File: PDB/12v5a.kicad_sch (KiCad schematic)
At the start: 28 parts, among them M3 CSD19502Q5B, M4 CSD17578Q3A, U21 LM5118MH/NOPB

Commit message: Finished all the footprints. doing poe myself now
finally.
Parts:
- added C40: 100nf, Capacitor_SMD:C_0603_1608Metric, symbol Device:C
- added D23: LED, LED_SMD:LED_0805_2012Metric, symbol Device:LED
- added F6: TR/3216FF15-R, Fuse:Fuse_1206_3216Metric, symbol Device:Fuse
- added R45: R_Shunt, Resistor_SMD:R_0603_1608Metric, symbol Device:R_Shunt
- added R46: 270, Capacitor_SMD:C_0603_1608Metric, symbol Device:R
- added TP11: TestPoint, TestPoint:TestPoint_Pad_D2.0mm, symbol Connector:TestPoint
- added U22: INA228, Package_SO:HVSSOP-10-1EP_3x3mm_P0.5mm_EP1.83x1.89mm, symbol Sensor_Energy:INA228
- Cboot4: renamed from Cboot1; footprint (none) -> Capacitor_SMD:C_0603_1608Metric
- Ccomp5: renamed from Ccomp3; footprint (none) -> Capacitor_SMD:C_0603_1608Metric
- Ccomp6: renamed from Ccomp4; footprint (none) -> Capacitor_SMD:C_0603_1608Metric
- Cin5: renamed from Cin1; footprint (none) -> Capacitor_SMD:C_0603_1608Metric
- Cin_1: renamed from Cin_2; footprint (none) -> Capacitor_SMD:C_0603_1608Metric
- Cin_2: renamed from Cin_3; footprint (none) -> Capacitor_SMD:C_0603_1608Metric
- Cinx4: renamed from Cinx1; footprint (none) -> Capacitor_SMD:C_0603_1608Metric
- Cout5: renamed from Cout1; footprint (none) -> Capacitor_SMD:C_0603_1608Metric
- Cout_2: renamed from Cout_3; footprint (none) -> Capacitor_SMD:C_0603_1608Metric
- Coutx4: renamed from Coutx3; footprint (none) -> Capacitor_SMD:C_0603_1608Metric
- Coutx5: renamed from Coutx4; footprint (none) -> Capacitor_SMD:C_0603_1608Metric
- Cramp3: renamed from Cramp1; footprint (none) -> Capacitor_SMD:C_0603_1608Metric
- Css3: renamed from Css1; footprint (none) -> Capacitor_SMD:C_0603_1608Metric
- Cvcc4: renamed from Cvcc1; footprint (none) -> Capacitor_SMD:C_0603_1608Metric
- D21: renamed from D20; footprint (none) -> Package_TO_SOT_SMD:TO-252-2_TabPin1
- D22: renamed from D21; footprint (none) -> Diode_THT:D_5W_P10.16mm_Horizontal
- L7: renamed from L4; footprint (none) -> Inductor_SMD:L_1206_3216Metric
- M3, M4: footprint (none) -> Dependencies:CSD19502Q5B
- Rcomp3: renamed from Rcomp1; footprint (none) -> Resistor_SMD:R_0603_1608Metric
- Renable3: renamed from Renable1; footprint (none) -> Resistor_SMD:R_0603_1608Metric
- Rfbb5: renamed from Rfbb1; footprint (none) -> Resistor_SMD:R_0603_1608Metric
- Rfbt5: renamed from Rfbt1; footprint (none) -> Resistor_SMD:R_0603_1608Metric
- Rsense3: renamed from Rsense1; footprint (none) -> Resistor_SMD:R_0603_1608Metric
- Rt3: renamed from Rt1; footprint (none) -> Resistor_SMD:R_0603_1608Metric
- Ruv5: renamed from Ruv3; footprint (none) -> Resistor_SMD:R_0603_1608Metric
- Ruv6: renamed from Ruv4; footprint (none) -> Resistor_SMD:R_0603_1608Metric
- U21: footprint (none) -> Dependencies:LM5118MH
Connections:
- net 12V@5A: now also R45.4, R46.1, TP11.1; no longer Cout5.1 (+), Cout_2.1 (+), Coutx4.1, Coutx5.1, D22.1 (K), Rfbt5.1, U21.10 (VOUT)
- net GND: now also C40.1, D23.1 (K), U22.1 (A1), U22.2 (A0), U22.7 (GND)
- new net: Cout5.1 (+), Cout_2.1 (+), Coutx4.1, Coutx5.1, D22.1 (K), F6.1, Rfbt5.1, U21.10 (VOUT)
- new net: D23.2 (A), R46.2
- new net: F6.2, R45.1, U22.8 (Vbus)
- new net: R45.2, U22.10 (Vin+)
- new net: R45.3, U22.9 (Vin-)
- new net +3.3V: C40.2, U22.6 (VS)
- new net SCL: U22.5 (SCL)
- new net SDA: U22.4 (SDA)
- no-connect marks 0 -> 1

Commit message: fixed component footprints
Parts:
- R45: footprint Resistor_SMD:R_0603_1608Metric -> Resistor_SMD:R_Shunt_Vishay_WSR2_WSR3_KelvinConnection
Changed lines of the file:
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@@
 		(dnp no)
 		(fields_autoplaced yes)
-		(property "Reference" "#PWR086"
+		(property "Reference" "#PWR097"
 			(at 524.51 81.28 0)
 			(hide yes)
@@
 			(project "PDB"
 				(path "/a9cf05c4-aac5-4cf1-b700-1d3045f8dfbd/9aa37ff9-47e7-4c71-b8fb-21d9fa084287"
-					(reference "#PWR086")
+					(reference "#PWR097")
 					(unit 1)
 				)
@@
 		(dnp no)
 		(fields_autoplaced yes)
-		(property "Reference" "#PWR082"
+		(property "Reference" "#PWR095"
 			(at 332.74 220.98 0)
 			(hide yes)
@@
 			(project "PDB"
 				(path "/a9cf05c4-aac5-4cf1-b700-1d3045f8dfbd/9aa37ff9-47e7-4c71-b8fb-21d9fa084287"
-					(reference "#PWR082")
+					(reference "#PWR095")
 					(unit 1)
 				)
@@
 		(dnp no)
 		(fields_autoplaced yes)
-		(property "Reference" "#PWR089"
+		(property "Reference" "#PWR0100"
 			(at 571.5 130.81 0)
 			(hide yes)
@@
 			(project "PDB"
 				(path "/a9cf05c4-aac5-4cf1-b700-1d3045f8dfbd/9aa37ff9-47e7-4c71-b8fb-21d9fa084287"
-					(reference "#PWR089")
+					(reference "#PWR0100")
 					(unit 1)
 				)
@@
 		(dnp no)
 		(fields_autoplaced yes)
-		(property "Reference" "#PWR087"
+		(property "Reference" "#PWR098"
 			(at 554.99 99.06 0)
 			(hide yes)
@@
 			(project "PDB"
 				(path "/a9cf05c4-aac5-4cf1-b700-1d3045f8dfbd/9aa37ff9-47e7-4c71-b8fb-21d9fa084287"
-					(reference "#PWR087")
+					(reference "#PWR098")
 					(unit 1)
 				)
@@
 		(dnp no)
 		(fields_autoplaced yes)
-		(property "Reference" "#PWR083"
+		(property "Reference" "#PWR099"
 			(at 548.64 121.92 0)
 			(hide yes)
@@
 			(project "PDB"
 				(path "/a9cf05c4-aac5-4cf1-b700-1d3045f8dfbd/9aa37ff9-47e7-4c71-b8fb-21d9fa084287"
-					(reference "#PWR083")
+					(reference "#PWR099")
 					(unit 1)
 				)
@@
 			)
 		)
-		(property "Footprint" "Resistor_SMD:R_0603_1608Metric"
+		(property "Footprint" "Resistor_SMD:R_Shunt_Vishay_WSR2_WSR3_KelvinConnection"
 			(at 534.67 119.888 90)
 			(hide yes)
@@
 		(dnp no)
 		(fields_autoplaced yes)
-		(property "Reference" "#PWR085"
+		(property "Reference" "#PWR094"
 			(at 297.18 101.6 0)
 			(hide yes)
@@
 			(project "PDB"
 				(path "/a9cf05c4-aac5-4cf1-b700-1d3045f8dfbd/9aa37ff9-47e7-4c71-b8fb-21d9fa084287"
-					(reference "#PWR085")
+					(reference "#PWR094")
 					(unit 1)
 				)
@@
 		(dnp no)
 		(fields_autoplaced yes)
-		(property "Reference" "#PWR081"
+		(property "Reference" "#PWR096"
 			(at 514.35 115.57 0)
 			(hide yes)
@@
 			(project "PDB"
 				(path "/a9cf05c4-aac5-4cf1-b700-1d3045f8dfbd/9aa37ff9-47e7-4c71-b8fb-21d9fa084287"
-					(reference "#PWR081")
+					(reference "#PWR096")
 					(unit 1)
 				)
@@
 		(dnp no)
 		(fields_autoplaced yes)
-		(property "Reference" "#PWR084"
+		(property "Reference" "#PWR093"
 			(at 229.87 256.54 0)
 			(hide yes)
@@
 			(project "PDB"
 				(path "/a9cf05c4-aac5-4cf1-b700-1d3045f8dfbd/9aa37ff9-47e7-4c71-b8fb-21d9fa084287"
-					(reference "#PWR084")
+					(reference "#PWR093")
 					(unit 1)
 				)
@@
 		(dnp no)
 		(fields_autoplaced yes)
-		(property "Reference" "#PWR080"
+		(property "Reference" "#PWR092"
 			(at 85.09 88.9 0)
 			(hide yes)
@@
 			(project "PDB"
 				(path "/a9cf05c4-aac5-4cf1-b700-1d3045f8dfbd/9aa37ff9-47e7-4c71-b8fb-21d9fa084287"
-					(reference "#PWR080")
+					(reference "#PWR092")
 					(unit 1)
 				)

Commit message: coordinated labels in schem
Labeled all components to be Rxx, Cxx, ext forms through all sheets so labels for BOM and layout are work together as one long list.
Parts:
- renumbered Cramp3 to C68, Cin5 to C69, Css3 to C70, Cin_1 to C71, Cin_2 to C72, Cinx4 to C73, Ccomp5 to C74, Ccomp6 to C75, Cvcc4 to C76, Cboot4 to C77, Coutx4 to C78, Coutx5 to C79, Cout5 to C80, Cout_2 to C81, C40 to C82, M3 to Q11, M4 to Q12, Ruv5 to R63, Ruv6 to R64, Renable3 to R65, Rt3 to R66, Rcomp3 to R67, Rfbb5 to R68, Rfbt5 to R69, Rsense3 to R70, R45 to R71, R46 to R72

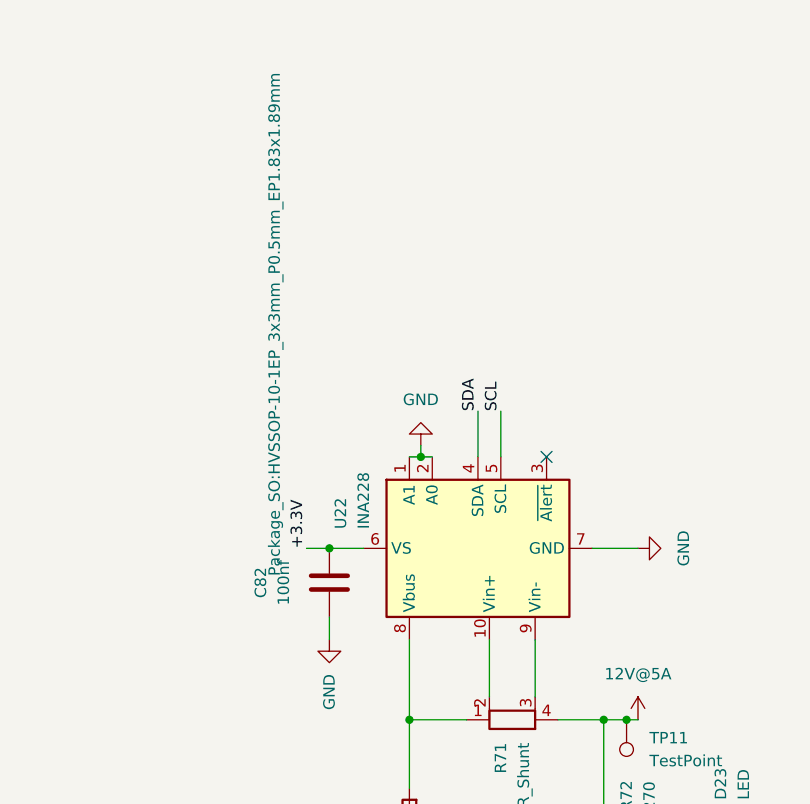
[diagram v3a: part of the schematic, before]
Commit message: last push before removing oring
i think we're going with an interlock system instead. the battery oring on here will take far too much physical room on the board to make it worthwhile. this push removes the oring and assumes a single power input.
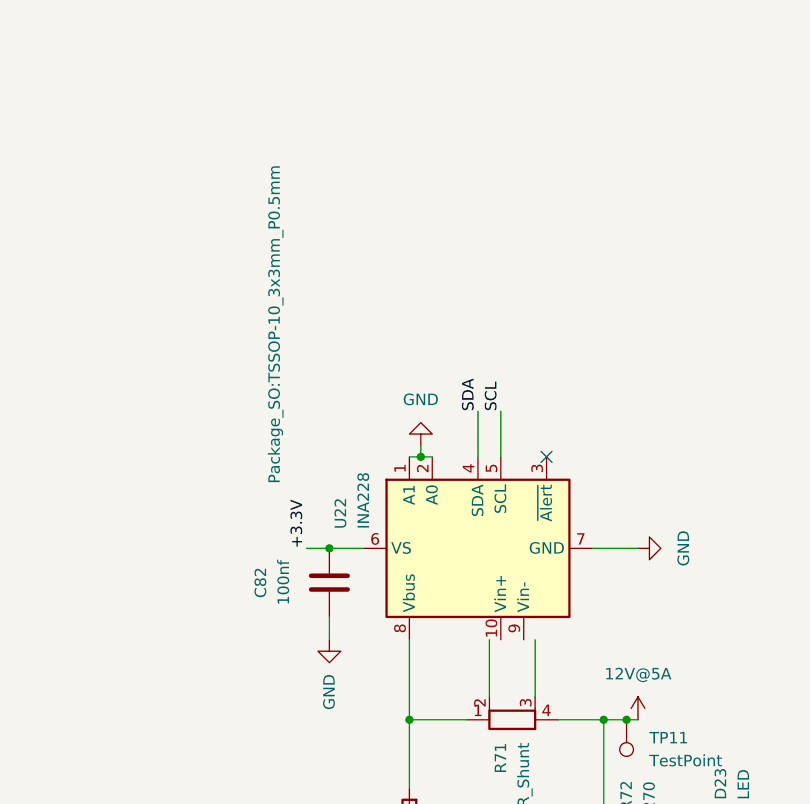
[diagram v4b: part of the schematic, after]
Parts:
- R71: footprint Resistor_SMD:R_Shunt_Vishay_WSR2_WSR3_KelvinConnection -> Resistor_SMD:R_Shunt_Vishay_WSK2512_6332Metric_T2.21mm
- U22: footprint Package_SO:HVSSOP-10-1EP_3x3mm_P0.5mm_EP1.83x1.89mm -> Package_SO:TSSOP-10_3x3mm_P0.5mm
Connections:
- net at R71.2: no longer U22.10 (Vin+)
- net at R71.3: no longer U22.9 (Vin-)
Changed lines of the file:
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@@
 			)
 		)
-		(property "Footprint" "Resistor_SMD:R_Shunt_Vishay_WSR2_WSR3_KelvinConnection"
+		(property "Footprint" "Resistor_SMD:R_Shunt_Vishay_WSK2512_6332Metric_T2.21mm"
 			(at 534.67 119.888 90)
 			(hide yes)
@@
 			)
 		)
-		(property "Footprint" "Package_SO:HVSSOP-10-1EP_3x3mm_P0.5mm_EP1.83x1.89mm"
+		(property "Footprint" "Package_SO:TSSOP-10_3x3mm_P0.5mm"
 			(at 508.254 74.168 0)
 			(show_name no)
